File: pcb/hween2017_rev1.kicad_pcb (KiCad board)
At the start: 2 copper layers, 86.4 x 66 mm, 36 parts, among them J1 BATTERY, J2 JTAG, K1 SY-3W-K, K2 SY-3W-K, U1 HV509, U2 MSP430FR2100IPW

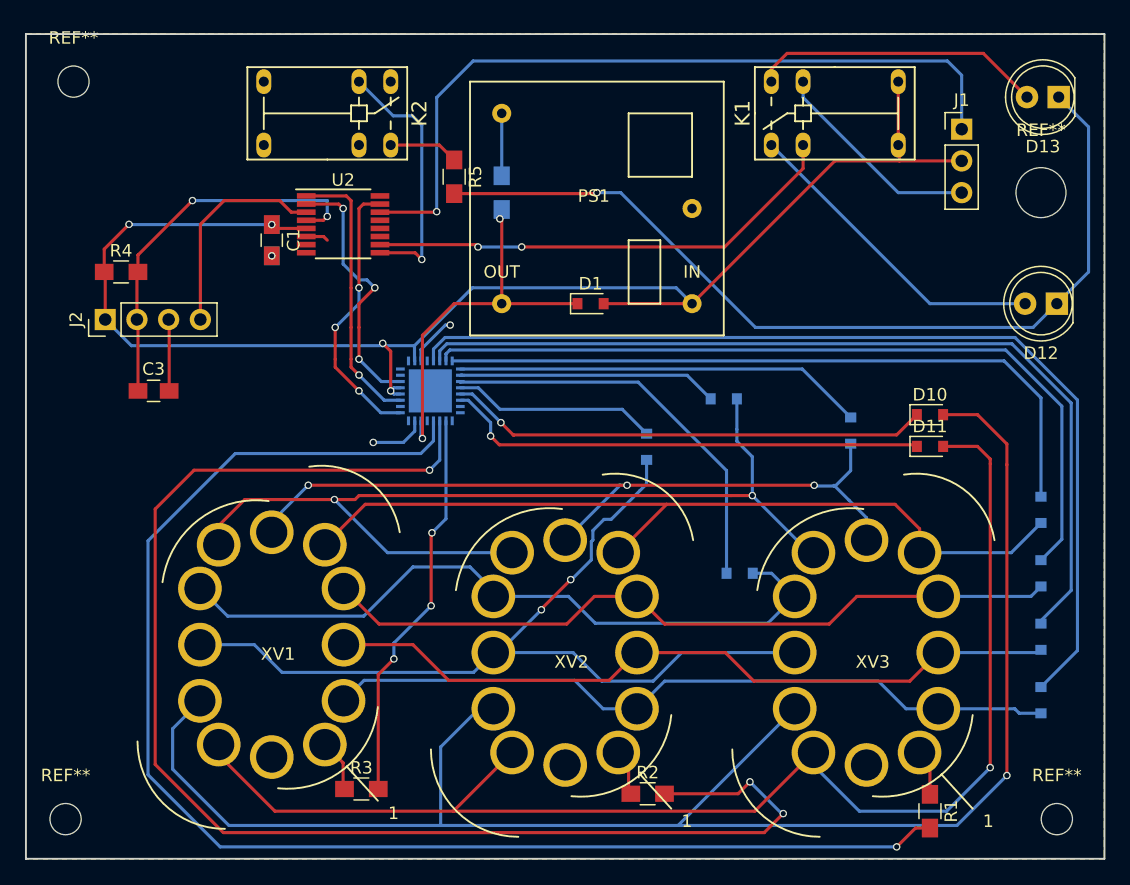
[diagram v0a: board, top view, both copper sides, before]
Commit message: Add new PCB changes and a stencil STL file.
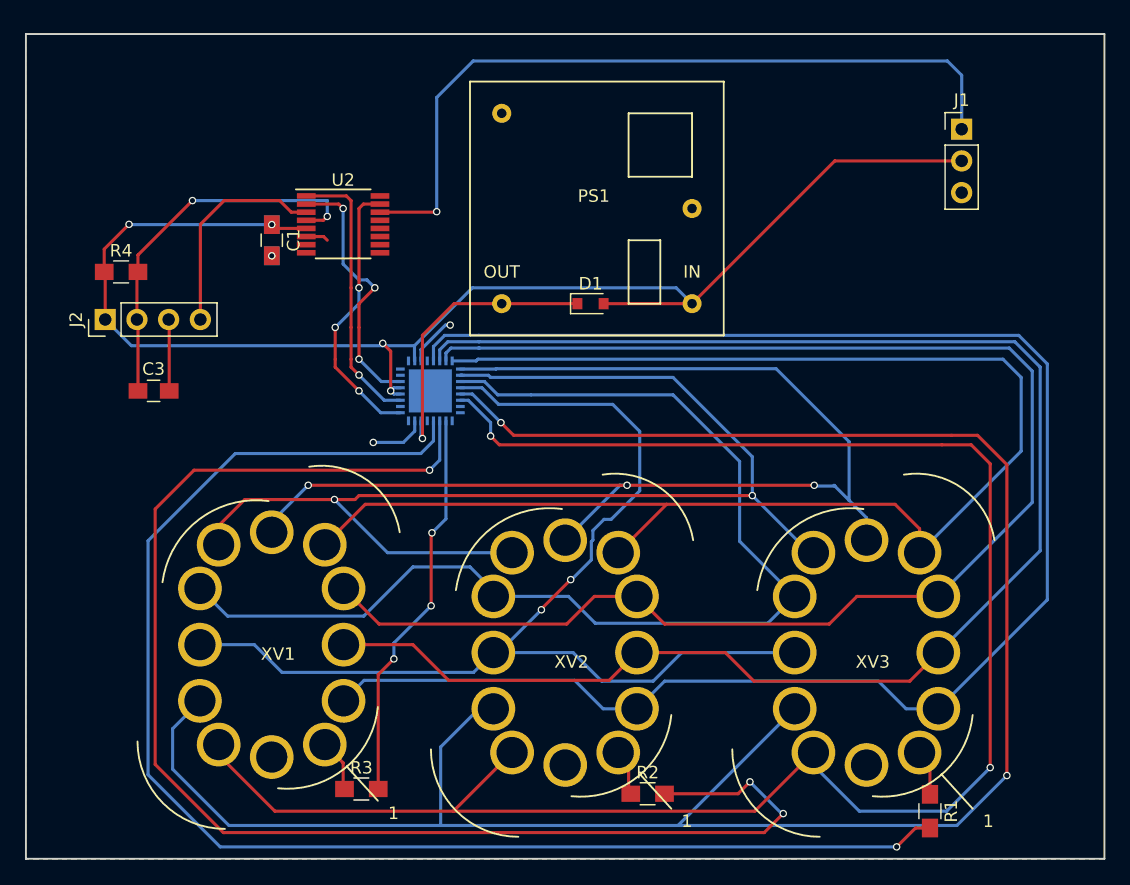
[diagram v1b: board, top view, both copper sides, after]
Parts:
- removed D10, D11, D2, D3, D4, D5, D6, D7, D8, D9: D, Diodes_SMD:D_0805
- removed D12, D13: LED, LEDs:LED_D5.0mm
- removed K1, K2: SY-3W-K, halloween:Fujitsu_Relay_SY-3W-K_SPDT_12.5x7.4
- removed R5: 1 k, Resistors_SMD:R_0805_HandSoldering
- removed R6: 100k, Resistors_SMD:R_0805_HandSoldering
- removed REF**: MountingHole_4mm, Mounting_Holes:MountingHole_4mm
- removed REF** (x3): MountingHole_2.5mm, Mounting_Holes:MountingHole_2.5mm
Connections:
- U1 pad 1: Net-(D6-Pad1) -> /if_6
- U1 pad 2: Net-(D7-Pad1) -> /if_5
- U1 pad 29: Net-(D2-Pad1) -> /if_0
- U1 pad 3: Net-(D8-Pad1) -> /if_4
- U1 pad 30: Net-(D3-Pad1) -> /if_9
- U1 pad 31: Net-(D4-Pad1) -> /if_8
- U1 pad 32: Net-(D5-Pad1) -> /if_7
- U1 pad 4: Net-(D9-Pad1) -> /if_3
- U1 pad 5: Net-(D10-Pad1) -> /if_2
- U1 pad 6: Net-(D11-Pad1) -> /if_1
- U2 pad 10: L_IN -> Net-(U2-Pad10)
- U2 pad 9: L_OUT -> Net-(U2-Pad9)
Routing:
- net Net-(D2-Pad1): track 79.2 -> 0.00 mm
- net /if_0: track 59.5 -> 134.0 mm
- net Net-(D3-Pad1): track 72.2 -> 0.00 mm
- net Net-(D12-Pad1): track 72.1 -> 0.00 mm, vias 1 -> 0
- net /if_9: track 59.9 -> 128.0 mm
- net Net-(D4-Pad1): track 64.9 -> 0.00 mm
- net /if_8: track 60.1 -> 121.3 mm
- net Net-(D5-Pad1): track 56.3 -> 0.00 mm
- net /if_7: track 67.9 -> 120.8 mm
- net /if_1: track 106.0 -> 146.6 mm, vias 1 -> 2
- net Net-(D11-Pad1): track 38.7 -> 0.00 mm, vias 1 -> 0
- net Net-(D10-Pad1): track 38.6 -> 0.00 mm, vias 1 -> 0
- net L_IN: track 38.4 -> 0.00 mm, vias 2 -> 0
- net /if_2: track 134.3 -> 172.7 mm, vias 1 -> 2
- net /if_6: track 63.6 -> 97.8 mm
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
